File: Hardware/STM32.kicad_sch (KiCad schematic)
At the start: 49 parts, among them IC1 STTS22HTR, U3 STM32L4R5ZITx

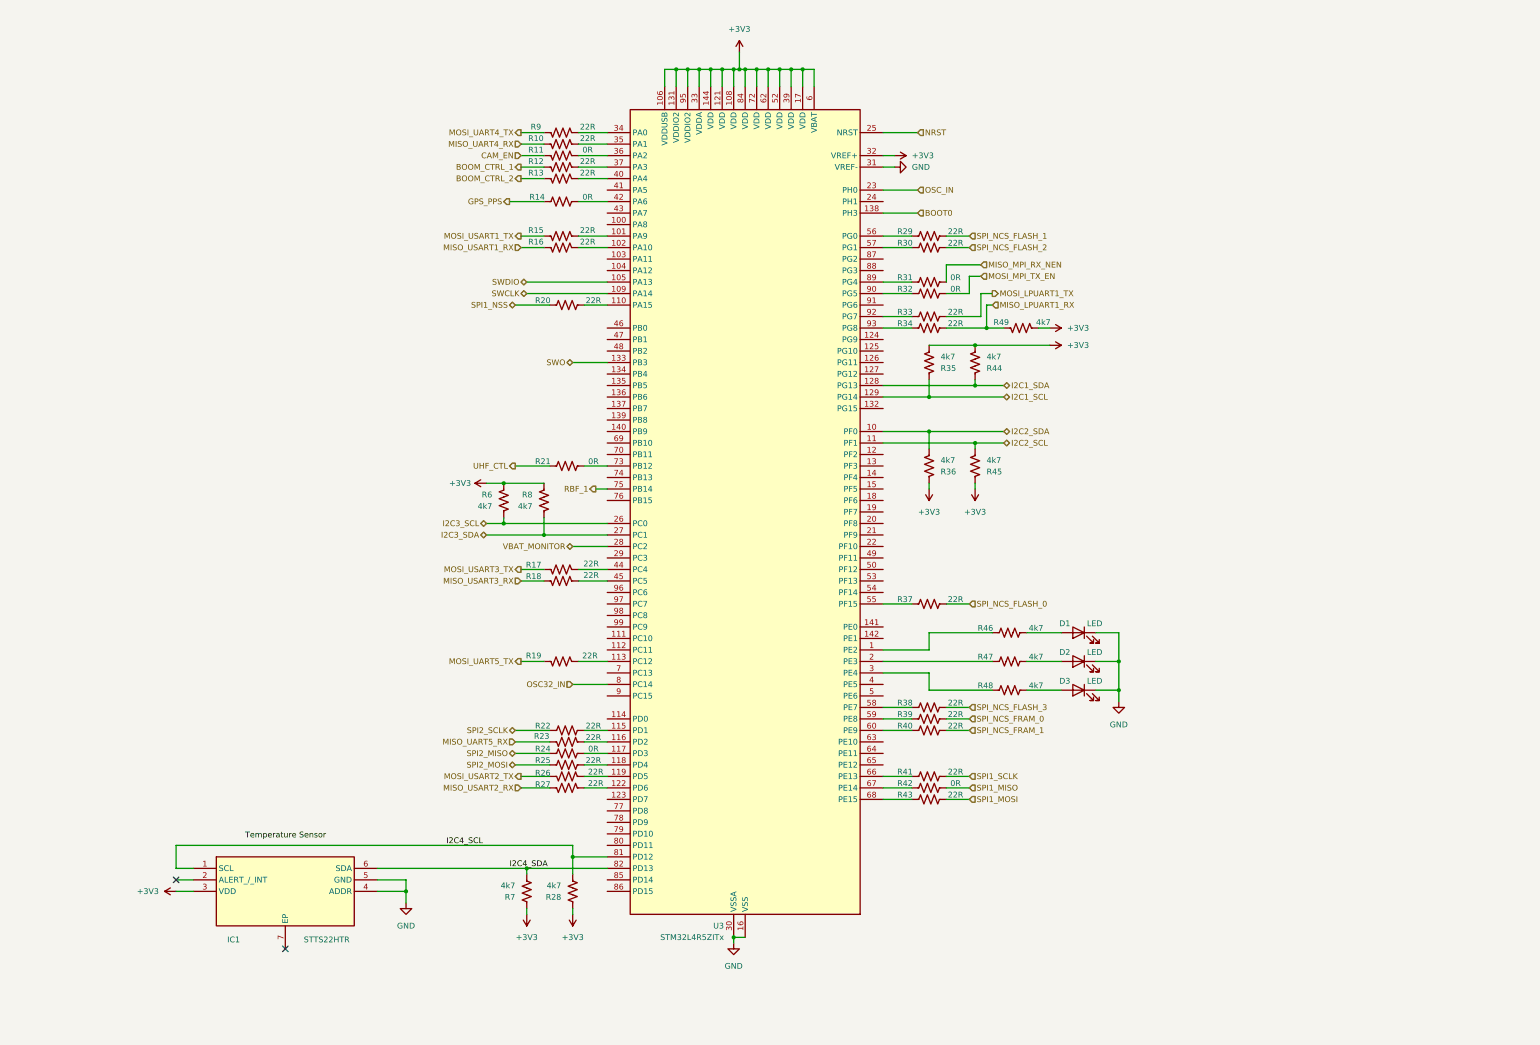
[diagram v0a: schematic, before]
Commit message: Add fast clock
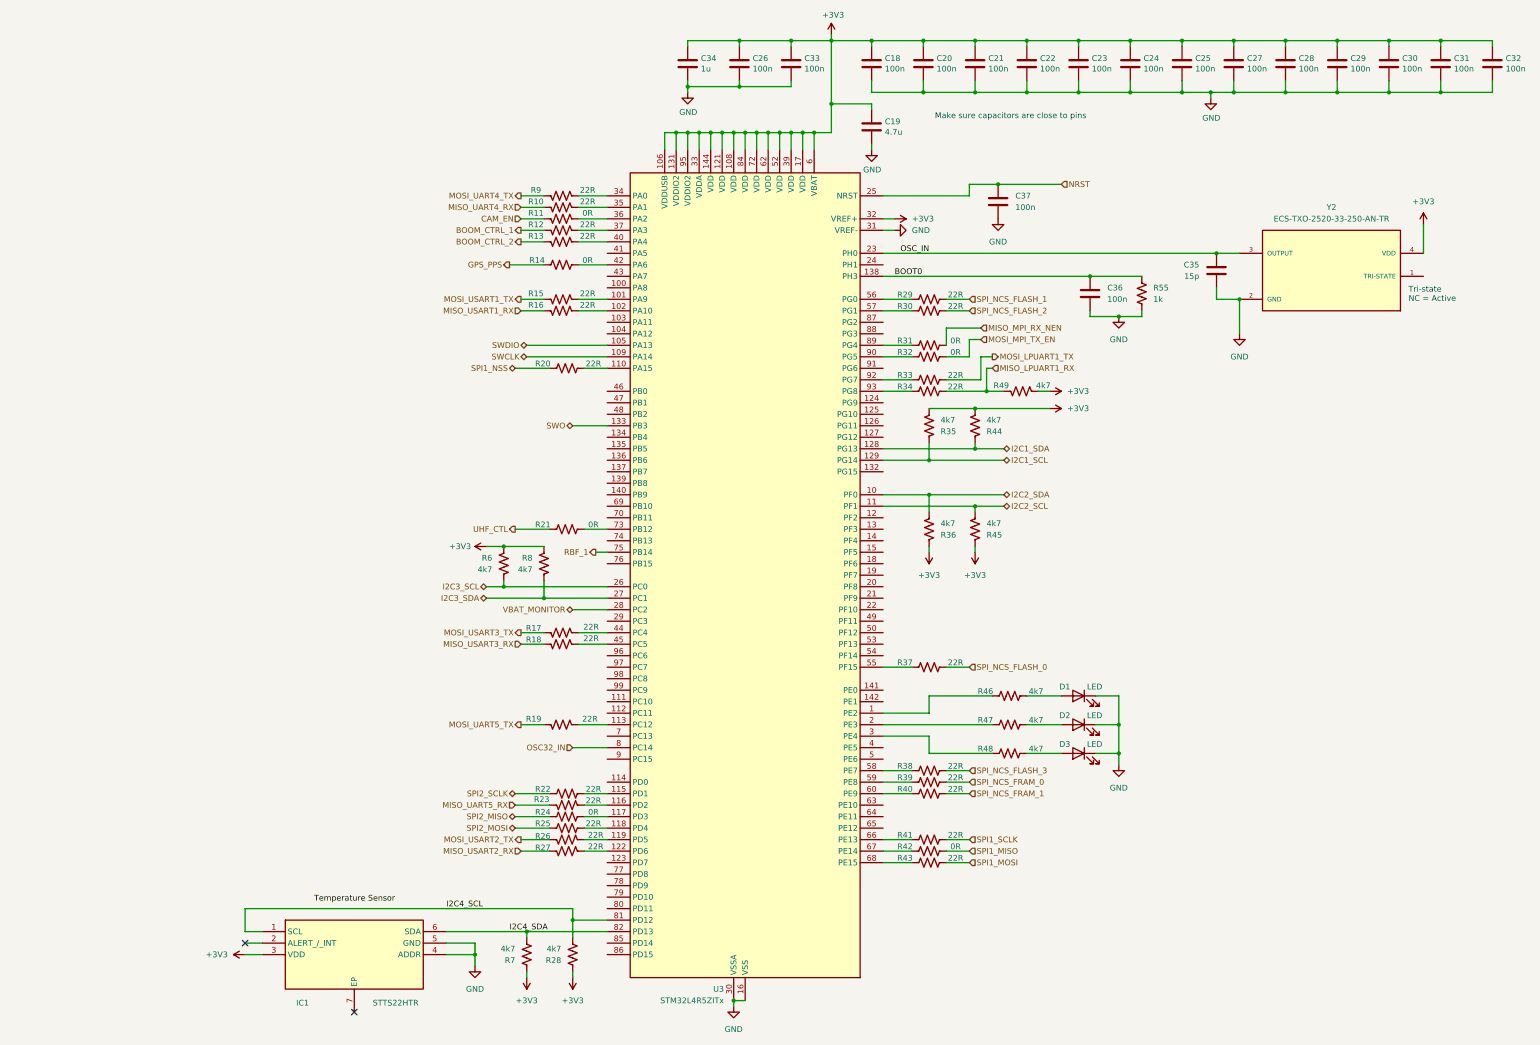
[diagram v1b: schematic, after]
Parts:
- added C18, C20, C21, C22, C23, C24, C25, C26, C27, C28, C29, C30, C31, C32, C33: 100n, Capacitor_SMD:C_0402_1005Metric, symbol Device:C
- added C19: 4.7u, Capacitor_SMD:C_0402_1005Metric, symbol Device:C
- added C34: 1u, Capacitor_SMD:C_0402_1005Metric, symbol Device:C
- added C35: 15p, symbol Device:C
- added C36, C37: 100n, symbol Device:C
- added R55: 1k, symbol Device:R_US
- added Y2: ECS-TXO-2520-33-250-AN-TR, ECS-TXO-2520-33-250-AN-TR:OSC_ECS-TXO-2520-33-250-AN-TR, symbol ECS-TXO-2520-33-250-AN-TR:ECS-TXO-2520-33-250-AN-TR
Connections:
- net +3V3: now also C18.1, C19.1, C20.1, C21.1, C22.1, C23.1, C24.1, C25.1, C26.1, C27.1, C28.1, C29.1, C30.1, C31.1, C32.1, C33.1, C34.1, Y2.4 (VDD)
- net BOOT0: now also C36.1, R55.1
- net GND: now also C18.2, C19.2, C20.2, C21.2, C22.2, C23.2, C24.2, C25.2, C26.2, C27.2, C28.2, C29.2, C30.2, C31.2, C32.2, C33.2, C34.2, C35.2, C36.2, C37.2, R55.2, Y2.2 (GND)
- net NRST: now also C37.1
- net OSC_IN: now also C35.1, Y2.3 (OUTPUT)
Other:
- note added: "Make sure capacitors are close to pins"
- note added: "Tri-state NC = Active"
- moved on the sheet: D1, D2, D3, IC1, R10, R11, R12, R13, R14, R15, R16, R17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

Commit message: STM32 Flash Memory
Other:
- added sheet Flash Memory (stm32_flash.kicad_sch)
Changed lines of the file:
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@@
+		)
+	)
+	(sheet
+		(at 54.61 139.7)
+		(size 40.64 13.97)
+		(exclude_from_sim no)
+		(in_bom yes)
+		(on_board yes)
+		(dnp no)
+		(fields_autoplaced yes)
+		(stroke
+			(width 0.1524)
+			(type solid)
+		)
+		(fill
+			(color 0 0 0 0.0000)
+		)
+		(property "Sheetname" "Flash Memory"
+			(at 54.61 138.9884 0)
+			(effects
+				(font
+					(size 1.27 1.27)
+				)
+				(justify left bottom)
+			)
+		)
+		(property "Sheetfile" "stm32_flash.kicad_sch"
+			(at 54.61 154.2546 0)
+			(effects
+				(font
+					(size 1.27 1.27)
+				)
+				(justify left top)
+			)
+		)
+		(pin "SPI_NCS_FLASH_3" input
+			(at 95.25 149.86 0)
+			(effects
+				(font
+					(size 1.27 1.27)
+				)
+				(justify right)
+			)
+		)
+		(pin "SPI_FLASH_MISO" output
+			(at 54.61 144.78 180)
+			(effects
+				(font
+					(size 1.27 1.27)
+				)
+				(justify left)
+			)
+		)
+		(pin "SPI_NCS_FLASH_1" input
+			(at 95.25 144.78 0)
+			(effects
+				(font
+					(size 1.27 1.27)
+				)
+				(justify right)
+			)
+		)
+		(pin "SPI_FLASH_SCLK" output
+			(at 54.61 142.24 180)
+			(effects
+				(font
+					(size 1.27 1.27)
+				)
+				(justify left)
+			)
+		)
+		(pin "SPI_NCS_FLASH_2" input
+			(at 95.25 147.32 0)
+			(effects
+				(font
+					(size 1.27 1.27)
+				)
+				(justify right)
+			)
+		)
+		(pin "SPI_FLASH_MOSI" output
+			(at 54.61 147.32 180)
+			(effects
+				(font
+					(size 1.27 1.27)
+				)
+				(justify left)
+			)
+		)
+		(pin "SPI_NCS_FLASH_0" input
+			(at 95.25 142.24 0)
+			(effects
+				(font
+					(size 1.27 1.27)
+				)
+				(justify right)
+			)
+		)
+		(instances
+			(project "CTS-SAT-2-OBC-PCB"
+				(path "/58243925-df8d-4fc1-899e-fce866d1d25a/c7b2a9f5-c39c-4892-aa33-31b3626fafef"
+					(page "5")
+				)
+			)
 		)
 	)

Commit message: STM32 RTC
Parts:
- added C42: 100n, Capacitor_SMD:C_0402_1005Metric, symbol Device:C
- added Y3: TG-3541CE_32.7680KXB3, TG3541CE327680KXB3, symbol TG-3541CE_32.7680KXB3:TG-3541CE_32.7680KXB3
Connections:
- net +3V3: now also C42.1, Y3.1 (OE), Y3.2 (VCC_1), Y3.3 (VCC_2)
- net GND: now also C42.2, Y3.5 (GND_1), Y3.7 (GND_2), Y3.8 (GND_3), Y3.9 (GND_4)
- net I2C4_SCL: now also R7.2; no longer R28.2
- net I2C4_SDA: now also R28.2; no longer R7.2
- net OSC32_IN: now also Y3.4 (OUT)
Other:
- removed sheet Flash Memory
- moved on the sheet: IC1, R28, R7

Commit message: Connect connectors
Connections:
- net DEBUG_LED: now reaches R46.1, U3.1 (PE2)
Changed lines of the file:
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@@
 	)
 	(junction
+		(at 265.43 184.15)
+		(diameter 0)
+		(color 0 0 0 0)
+	)
+	(junction
 		(at 232.41 59.69)
 		(diameter 0)
@@
 	(wire
 		(pts
+			(xy 265.43 181.61) (xy 265.43 184.15)
+		)
+		(stroke
+			(width 0)
+			(type default)
+		)
+	)
+	(wire
+		(pts
 			(xy 245.11 40.64) (xy 245.11 39.37)
 		)
@@
 	(wire
 		(pts
-			(xy 257.81 184.15) (xy 271.78 184.15)
+			(xy 257.81 184.15) (xy 265.43 184.15)
 		)
 		(stroke
@@
 	(wire
 		(pts
+			(xy 262.89 181.61) (xy 265.43 181.61)
+		)
+		(stroke
+			(width 0)
+			(type default)
+		)
+	)
+	(wire
+		(pts
 			(xy 146.05 222.25) (xy 146.05 223.52)
 		)
@@
 		)
 	)
+	(wire
+		(pts
+			(xy 265.43 184.15) (xy 271.78 184.15)
+		)
+		(stroke
+			(width 0)
+			(type default)
+		)
+	)
 	(label "Temperature Sensor"
 		(at 105.41 229.87 0)
@@
 		)
 	)
+	(hierarchical_label "DEBUG_LED"
+		(shape output)
+		(at 262.89 181.61 180)
+		(effects
+			(font
+				(size 1.27 1.27)
+			)
+			(justify right)
+		)
+	)
 	(hierarchical_label "BOOM_CTRL_1"
 		(shape output)
@@
 		(on_board yes)
 		(dnp no)
-		(property "Reference" "#PWR051"
+		(property "Reference" "#PWR51"
 			(at 320.04 58.42 0)
 			(effects
@@
 		)
 		(property "Value" "GND"
-			(at 320.167 56.4642 0)
+			(at 320.04 55.88 0)
 			(effects
 				(font
@@
 			)
 		)
-		(property "Description" ""
+		(property "Description" "Power symbol creates a global label with name \"GND\" , ground"
 			(at 320.04 52.07 0)
 			(effects
@@
 					(size 1.27 1.27)
 				)
+				(hide yes)
 			)
 		)
@@
 			(project "CTS-SAT-2-OBC-PCB"
 				(path "/58243925-df8d-4fc1-899e-fce866d1d25a/c7b2a9f5-c39c-4892-aa33-31b3626fafef"
-					(reference "#PWR051")
+					(reference "#PWR51")
 					(unit 1)
 				)
@@
 		(dnp no)
 		(fields_autoplaced yes)
-		(property "Reference" "#PWR024"
+		(property "Reference" "#PWR24"
 			(at 256.54 81.28 0)
 			(effects
@@
 			(project "CTS-SAT-2-OBC-PCB"
 				(path "/58243925-df8d-4fc1-899e-fce866d1d25a/c7b2a9f5-c39c-4892-aa33-31b3626fafef"
-					(reference "#PWR024")
+					(reference "#PWR24")
 					(unit 1)
 				)
@@
 		(dnp no)
 		(fields_autoplaced yes)
-		(property "Reference" "#PWR073"
+		(property "Reference" "#PWR73"
 			(at 143.51 208.28 0)
 			(effects
@@
 			(project "CTS-SAT-2-OBC-PCB"
 				(path "/58243925-df8d-4fc1-899e-fce866d1d25a/c7b2a9f5-c39c-4892-aa33-31b3626fafef"
-					(reference "#PWR073")
+					(reference "#PWR73")
 					(unit 1)
 				)
@@
 		(dnp no)
 		(fields_autoplaced yes)
-		(property "Reference" "#PWR017"
+		(property "Reference" "#PWR17"
 			(at 139.7 250.19 0)
 			(effects
@@
 			(project "CTS-SAT-2-OBC-PCB"
 				(path "/58243925-df8d-4fc1-899e-fce866d1d25a/c7b2a9f5-c39c-4892-aa33-31b3626fafef"
-					(reference "#PWR017")
+					(reference "#PWR17")
 					(unit 1)
 				)
@@
 		(dnp no)
 		(fields_autoplaced yes)
-		(property "Reference" "#PWR055"
+		(property "Reference" "#PWR55"
 			(at 273.05 85.09 0)
 			(effects
@@
 			(project "CTS-SAT-2-OBC-PCB"
 				(path "/58243925-df8d-4fc1-899e-fce866d1d25a/c7b2a9f5-c39c-4892-aa33-31b3626fafef"
-					(reference "#PWR055")
+					(reference "#PWR55")
 					(unit 1)
 				)
@@
 		(dnp no)
 		(fields_autoplaced yes)
-		(property "Reference" "#PWR052"
+		(property "Reference" "#PWR52"
 			(at 326.39 106.68 0)
 			(effects
@@
 			(project "CTS-SAT-2-OBC-PCB"
 				(path "/58243925-df8d-4fc1-899e-fce866d1d25a/c7b2a9f5-c39c-4892-aa33-31b3626fafef"
-					(reference "#PWR052")
+					(reference "#PWR52")
 					(unit 1)
 				)
@@
 		(dnp no)
 		(fields_autoplaced yes)
-		(property "Reference" "#PWR054"
+		(property "Reference" "#PWR54"
 			(at 299.72 106.68 0)
 			(effects
@@
 			(project ""
 				(path "/58243925-df8d-4fc1-899e-fce866d1d25a/c7b2a9f5-c39c-4892-aa33-31b3626fafef"
-					(reference "#PWR054")
+					(reference "#PWR54")
 					(unit 1)
 				)
@@
 		(dnp no)
 		(fields_autoplaced yes)
-		(property "Reference" "#PWR074"
+		(property "Reference" "#PWR74"
 			(at 106.68 208.28 0)
 			(effects
@@
 			(project "CTS-SAT-2-OBC-PCB"
 				(path "/58243925-df8d-4fc1-899e-fce866d1d25a/c7b2a9f5-c39c-4892-aa33-31b3626fafef"
-					(reference "#PWR074")
+					(reference "#PWR74")
 					(unit 1)
 				)
@@
 		(on_board yes)
 		(dnp no)
-		(property "Reference" "#PWR050"
+		(property "Reference" "#PWR50"
 			(at 245.11 69.85 0)
 			(effects
@@
 		)
 		(property "Value" "GND"
-			(at 245.237 67.8942 0)
+			(at 245.11 67.31 0)
 			(effects
 				(font
@@
 			)
 		)
-		(property "Description" ""
+		(property "Description" "Power symbol creates a global label with name \"GND\" , ground"
 			(at 245.11 63.5 0)
 			(effects
@@
 					(size 1.27 1.27)
 				)
+				(hide yes)
 			)
 		)
@@
 			(project "CTS-SAT-2-OBC-PCB"
 				(path "/58243925-df8d-4fc1-899e-fce866d1d25a/c7b2a9f5-c39c-4892-aa33-31b3626fafef"
-					(reference "#PWR050")
+					(reference "#PWR50")
 					(unit 1)
 				)
@@
 		(on_board yes)
 		(dnp no)
-		(property "Reference" "#PWR075"
+		(property "Reference" "#PWR75"
 			(at 157.48 189.23 0)
 			(effects
@@
 		)
 		(property "Value" "GND"
-			(at 157.607 187.2742 0)
+			(at 157.48 186.69 0)
 			(effects
 				(font
@@
 			)
 		)
-		(property "Description" ""
+		(property "Description" "Power symbol creates a global label with name \"GND\" , ground"
 			(at 157.48 182.88 0)
 			(effects
@@
 					(size 1.27 1.27)
 				)
+				(hide yes)
 			)
 		)
@@
 			(project "CTS-SAT-2-OBC-PCB"
 				(path "/58243925-df8d-4fc1-899e-fce866d1d25a/c7b2a9f5-c39c-4892-aa33-31b3626fafef"
-					(reference "#PWR075")
+					(reference "#PWR75")
 					(unit 1)
 				)
@@
 		(dnp no)
 		(fields_autoplaced yes)
-		(property "Reference" "#PWR021"
+		(property "Reference" "#PWR21"
 			(at 214.63 259.08 0)
 			(effects
@@
 			(project ""
 				(path "/58243925-df8d-4fc1-899e-fce866d1d25a/c7b2a9f5-c39c-4892-aa33-31b3626fafef"
-					(reference "#PWR021")
+					(reference "#PWR21")
 					(unit 1)
 				)
@@
 		(on_board yes)
 		(dnp no)
-		(property "Reference" "#PWR022"
+		(property "Reference" "#PWR22"
 			(at 204.47 57.15 0)
 			(effects
@@
 		)
 		(property "Value" "GND"
-			(at 204.597 55.1942 0)
+			(at 204.47 54.61 0)
 			(effects
 				(font
@@
 			)
 		)
-		(property "Description" ""
+		(property "Description" "Power symbol creates a global label with name \"GND\" , ground"
 			(at 204.47 50.8 0)
 			(effects
@@
 					(size 1.27 1.27)
 				)
+				(hide yes)
 			)
 		)
@@
 			(project "CTS-SAT-2-OBC-PCB"
 				(path "/58243925-df8d-4fc1-899e-fce866d1d25a/c7b2a9f5-c39c-4892-aa33-31b3626fafef"
-					(reference "#PWR022")
+					(reference "#PWR22")
 					(unit 1)
 				)
@@
 		(dnp no)
 		(fields_autoplaced yes)
-		(property "Reference" "#PWR029"
+		(property "Reference" "#PWR29"
 			(at 299.72 205.74 0)
 			(effects
@@
 			(project ""
 				(path "/58243925-df8d-4fc1-899e-fce866d1d25a/c7b2a9f5-c39c-4892-aa33-31b3626fafef"
-					(reference "#PWR029")
+					(reference "#PWR29")
 					(unit 1)
 				)
